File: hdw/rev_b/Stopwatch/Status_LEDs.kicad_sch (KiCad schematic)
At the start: 24 parts, among them U501 74LVC1G97, U502 74LVC1G97, U503 74LVC1G97, U504 74LVC1G97, U505 74LVC1G97

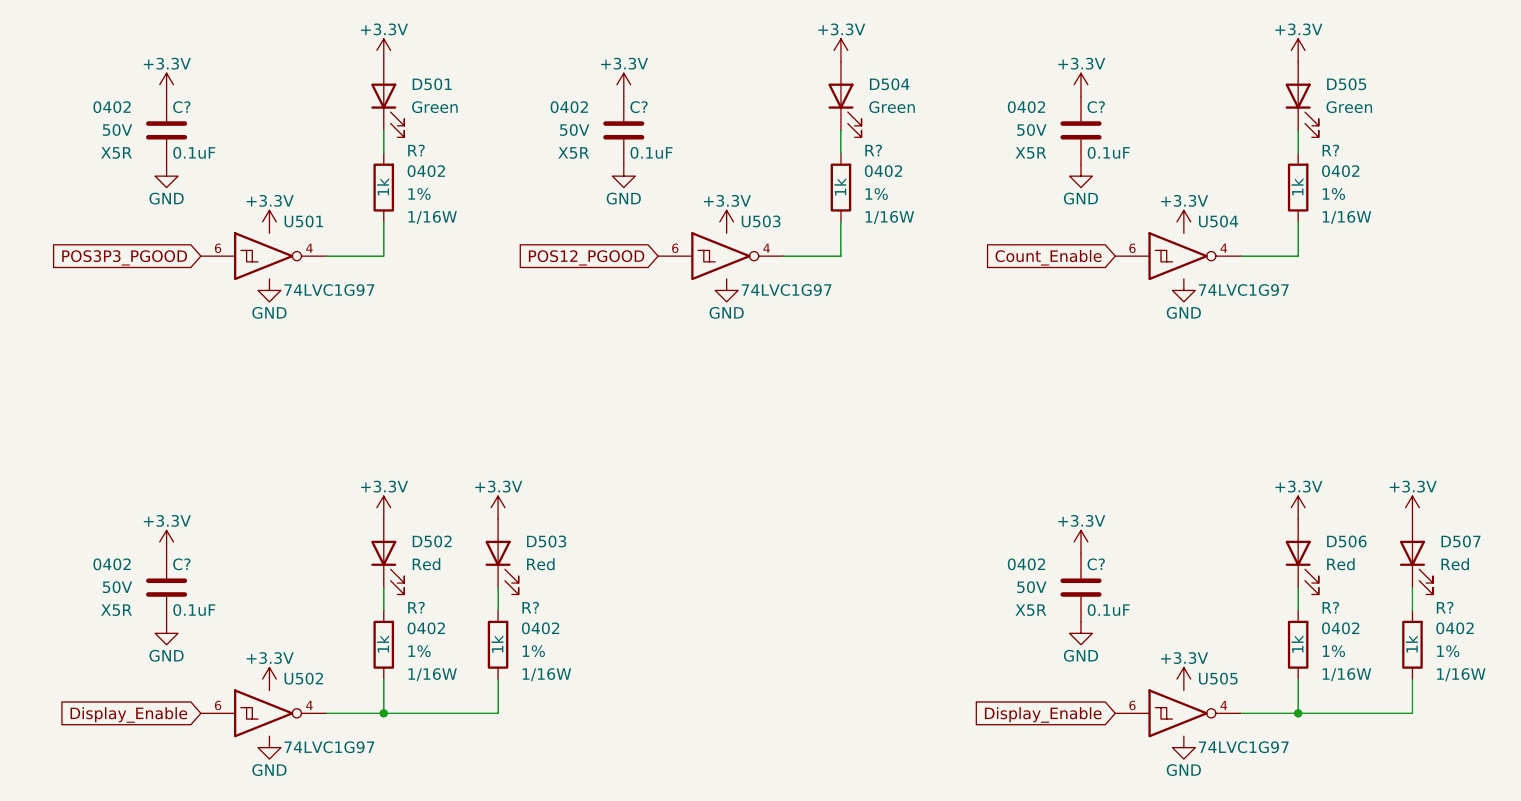
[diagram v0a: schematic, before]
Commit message: ported rev b to kicad 8
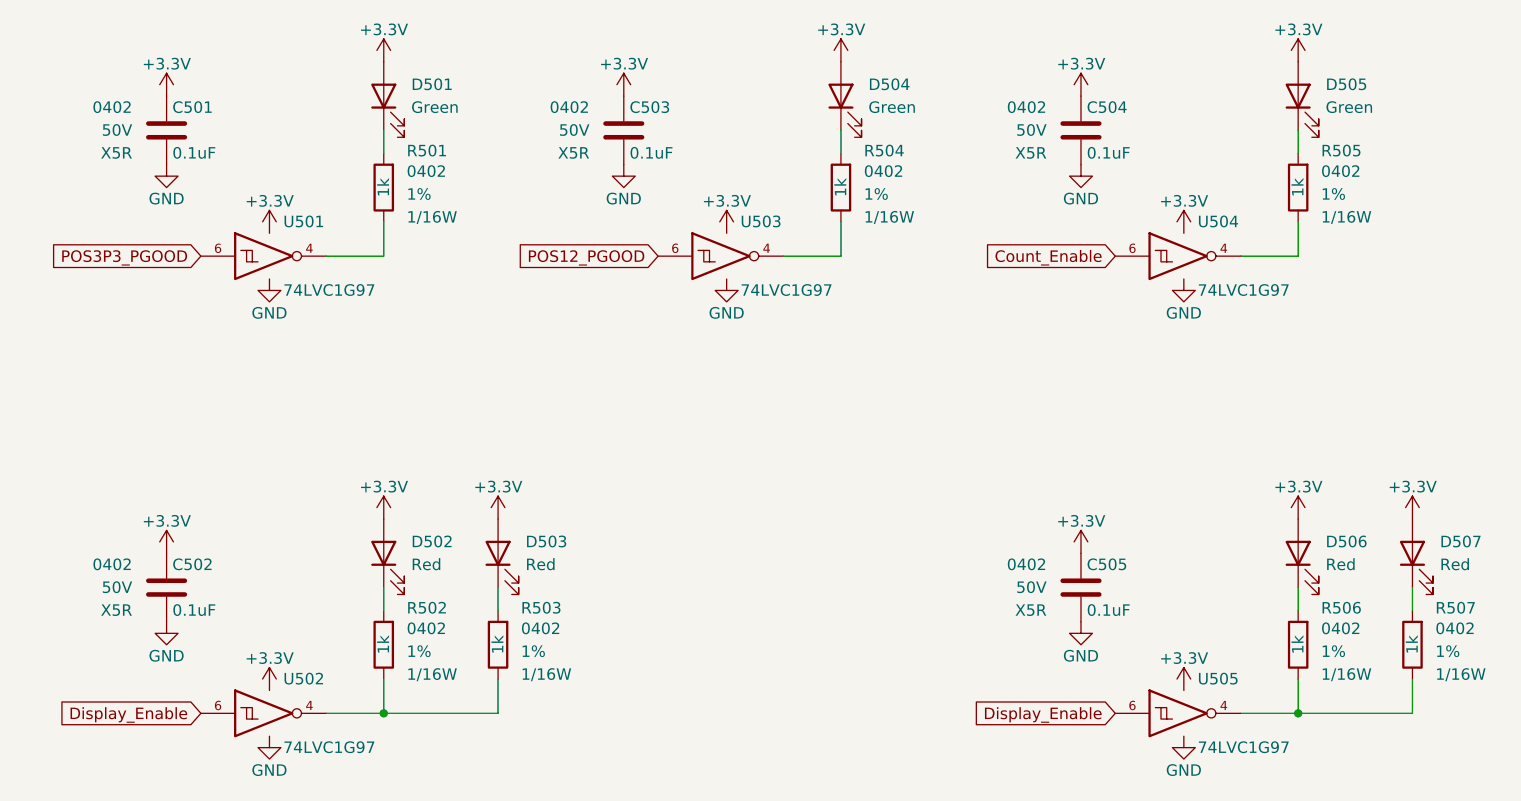
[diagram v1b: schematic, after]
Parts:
- gave numbers to parts that had none: 12

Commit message: integrated SC70 gates
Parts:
- U501, U502, U503, U504, U505: footprint Package_SON:Fairchild_MicroPak2-6_1.0x1.0mm_P0.35mm -> Package_TO_SOT_SMD:SOT-363_SC-70-6; Digi-Key PN 296-29875-1-ND -> 296-15582-1-ND
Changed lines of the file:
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@@
 			)
 		)
-		(property "Footprint" "Package_SON:Fairchild_MicroPak2-6_1.0x1.0mm_P0.35mm"
+		(property "Footprint" "Package_TO_SOT_SMD:SOT-363_SC-70-6"
 			(at 151.13 100.33 0)
 			(effects
@@
 			)
 		)
-		(property "Digi-Key PN" "296-29875-1-ND"
+		(property "Digi-Key PN" "296-15582-1-ND"
 			(at 149.86 100.33 0)
 			(effects
@@
 			)
 		)
-		(property "Footprint" "Package_SON:Fairchild_MicroPak2-6_1.0x1.0mm_P0.35mm"
+		(property "Footprint" "Package_TO_SOT_SMD:SOT-363_SC-70-6"
 			(at 49.53 100.33 0)
 			(effects
@@
 			)
 		)
-		(property "Digi-Key PN" "296-29875-1-ND"
+		(property "Digi-Key PN" "296-15582-1-ND"
 			(at 48.26 100.33 0)
 			(effects
@@
 			)
 		)
-		(property "Footprint" "Package_SON:Fairchild_MicroPak2-6_1.0x1.0mm_P0.35mm"
+		(property "Footprint" "Package_TO_SOT_SMD:SOT-363_SC-70-6"
 			(at 49.53 49.53 0)
 			(effects
@@
 			)
 		)
-		(property "Digi-Key PN" "296-29875-1-ND"
+		(property "Digi-Key PN" "296-15582-1-ND"
 			(at 48.26 49.53 0)
 			(effects
@@
 			)
 		)
-		(property "Footprint" "Package_SON:Fairchild_MicroPak2-6_1.0x1.0mm_P0.35mm"
+		(property "Footprint" "Package_TO_SOT_SMD:SOT-363_SC-70-6"
 			(at 151.13 49.53 0)
 			(effects
@@
 			)
 		)
-		(property "Digi-Key PN" "296-29875-1-ND"
+		(property "Digi-Key PN" "296-15582-1-ND"
 			(at 149.86 49.53 0)
 			(effects
@@
 			)
 		)
-		(property "Footprint" "Package_SON:Fairchild_MicroPak2-6_1.0x1.0mm_P0.35mm"
+		(property "Footprint" "Package_TO_SOT_SMD:SOT-363_SC-70-6"
 			(at 100.33 49.53 0)
 			(effects
@@
 			)
 		)
-		(property "Digi-Key PN" "296-29875-1-ND"
+		(property "Digi-Key PN" "296-15582-1-ND"
 			(at 99.06 49.53 0)
 			(effects
